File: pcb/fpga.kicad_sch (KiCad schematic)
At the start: 0 parts

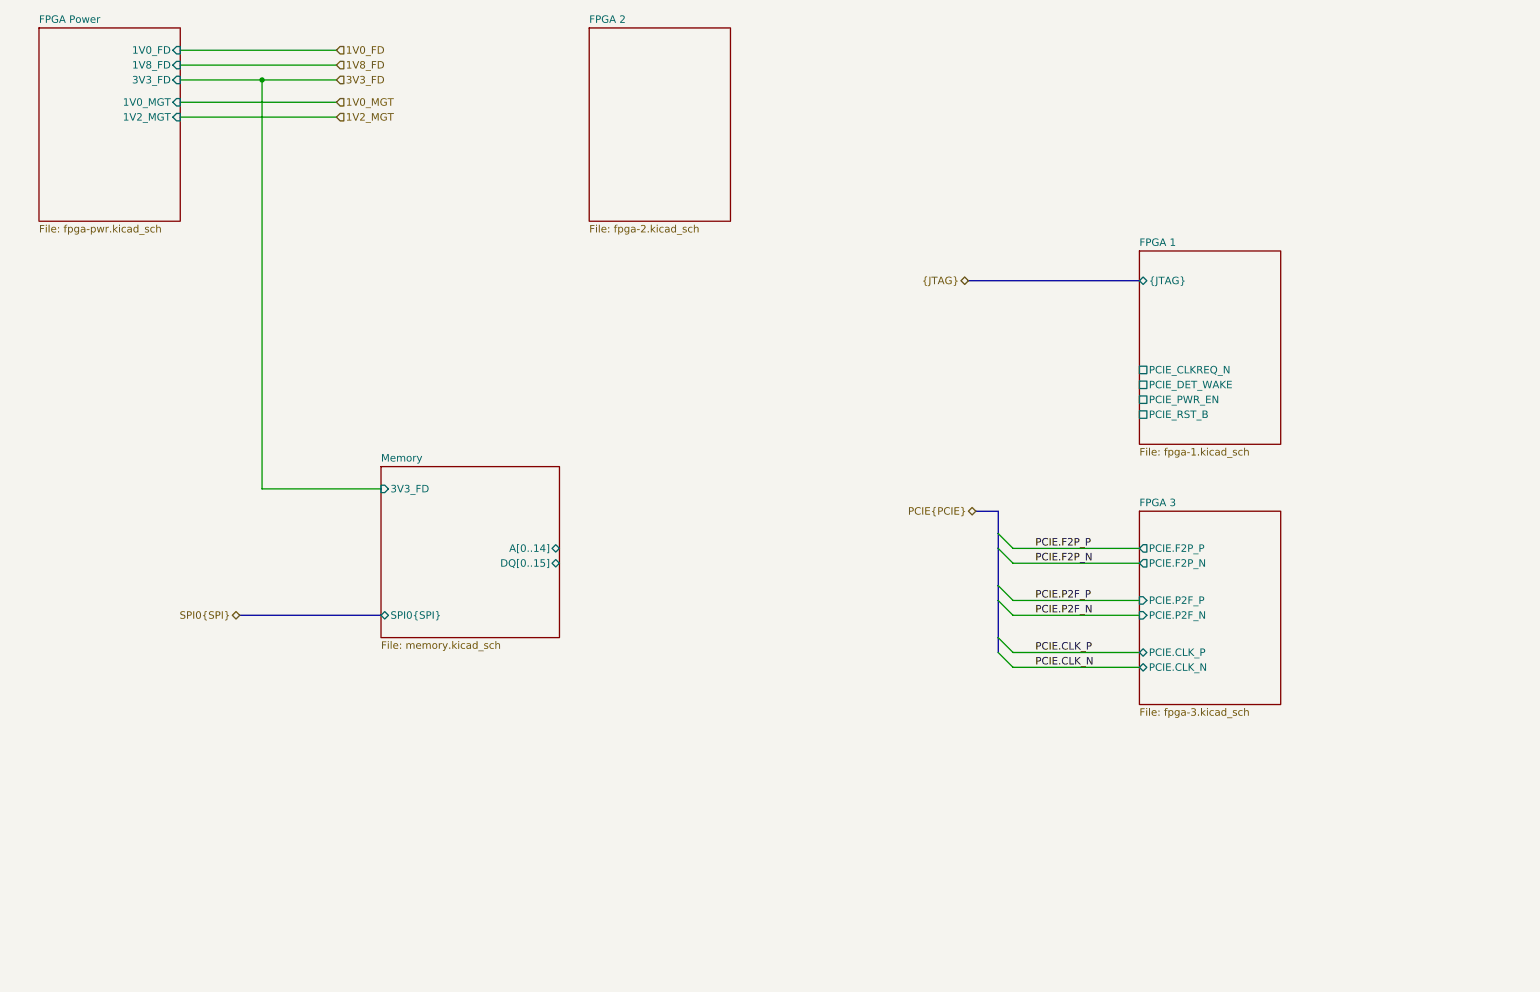
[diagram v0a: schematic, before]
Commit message: hierarchy and power sequencing, level shift
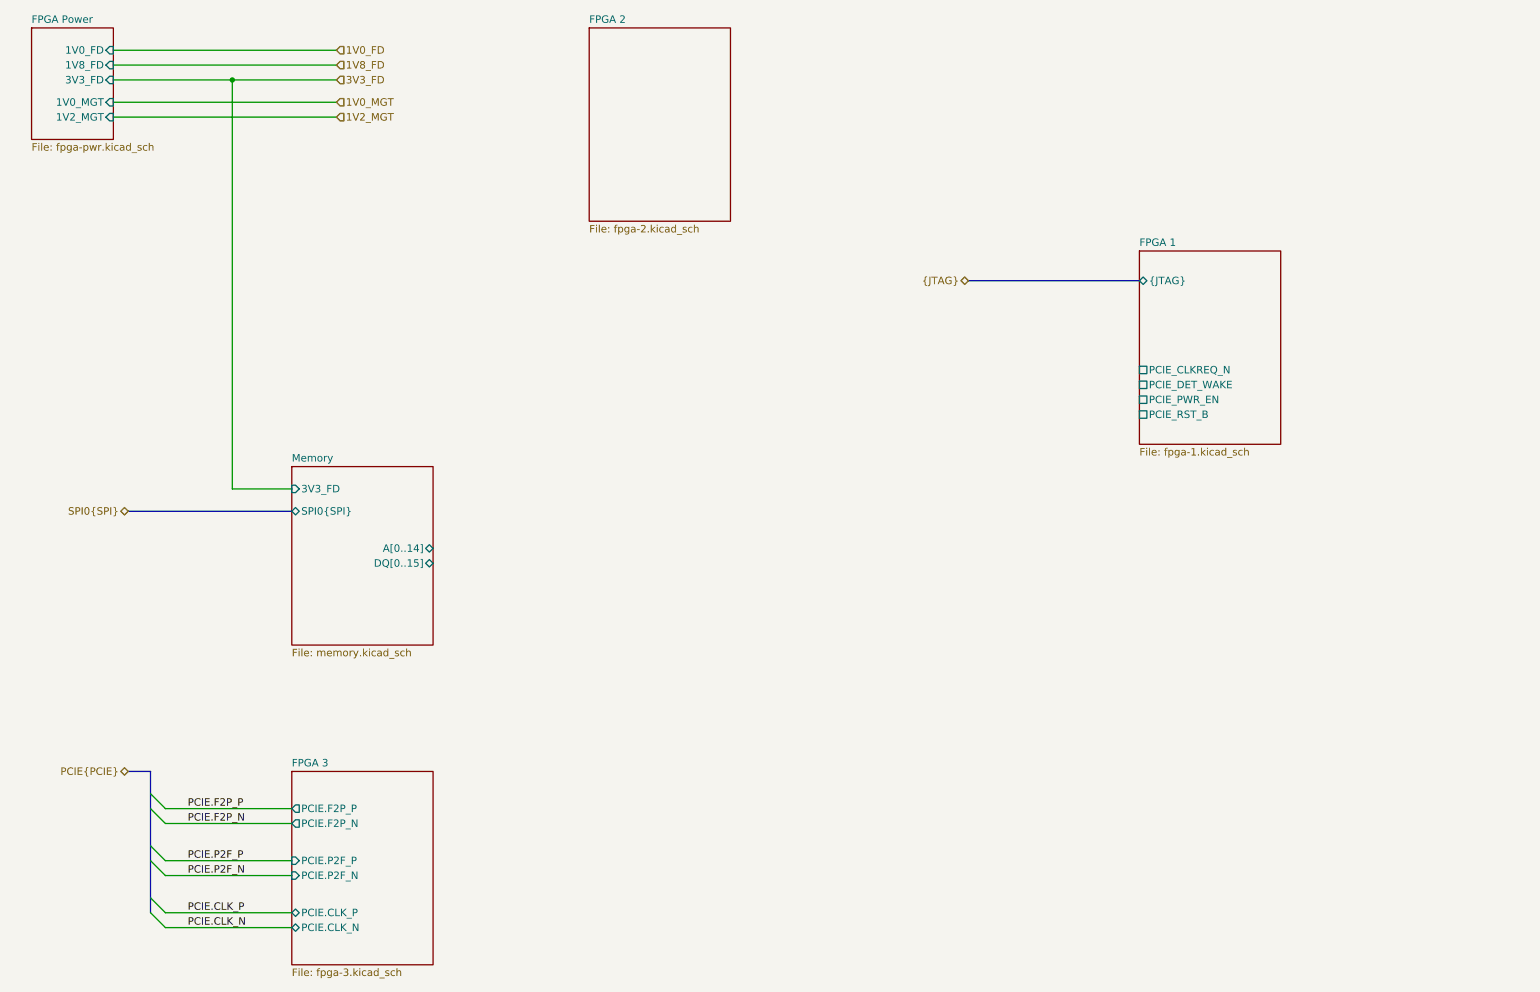
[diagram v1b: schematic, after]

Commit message: added hierarchical sheet, pwr seq
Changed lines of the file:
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@@
 	(bus
 		(pts
-			(xy 38.1 146.05) (xy 38.1 149.86)
+			(xy 38.1 132.08) (xy 38.1 149.86)
 		)
 		(stroke
@@
 	(bus
 		(pts
-			(xy 34.29 146.05) (xy 38.1 146.05)
+			(xy 34.29 132.08) (xy 38.1 132.08)
 		)
 		(stroke
@@
 		)
 	)
+	(hierarchical_label "PCIE.RST_B"
+		(shape input)
+		(at 34.29 134.62 180)
+		(effects
+			(font
+				(size 1.27 1.27)
+			)
+			(justify right)
+		)
+	)
 	(hierarchical_label "1V2_MGT"
 		(shape input)
@@
 	(hierarchical_label "PCIE{PCIE}"
 		(shape bidirectional)
-		(at 34.29 146.05 180)
+		(at 34.29 132.08 180)
 		(effects
 			(font

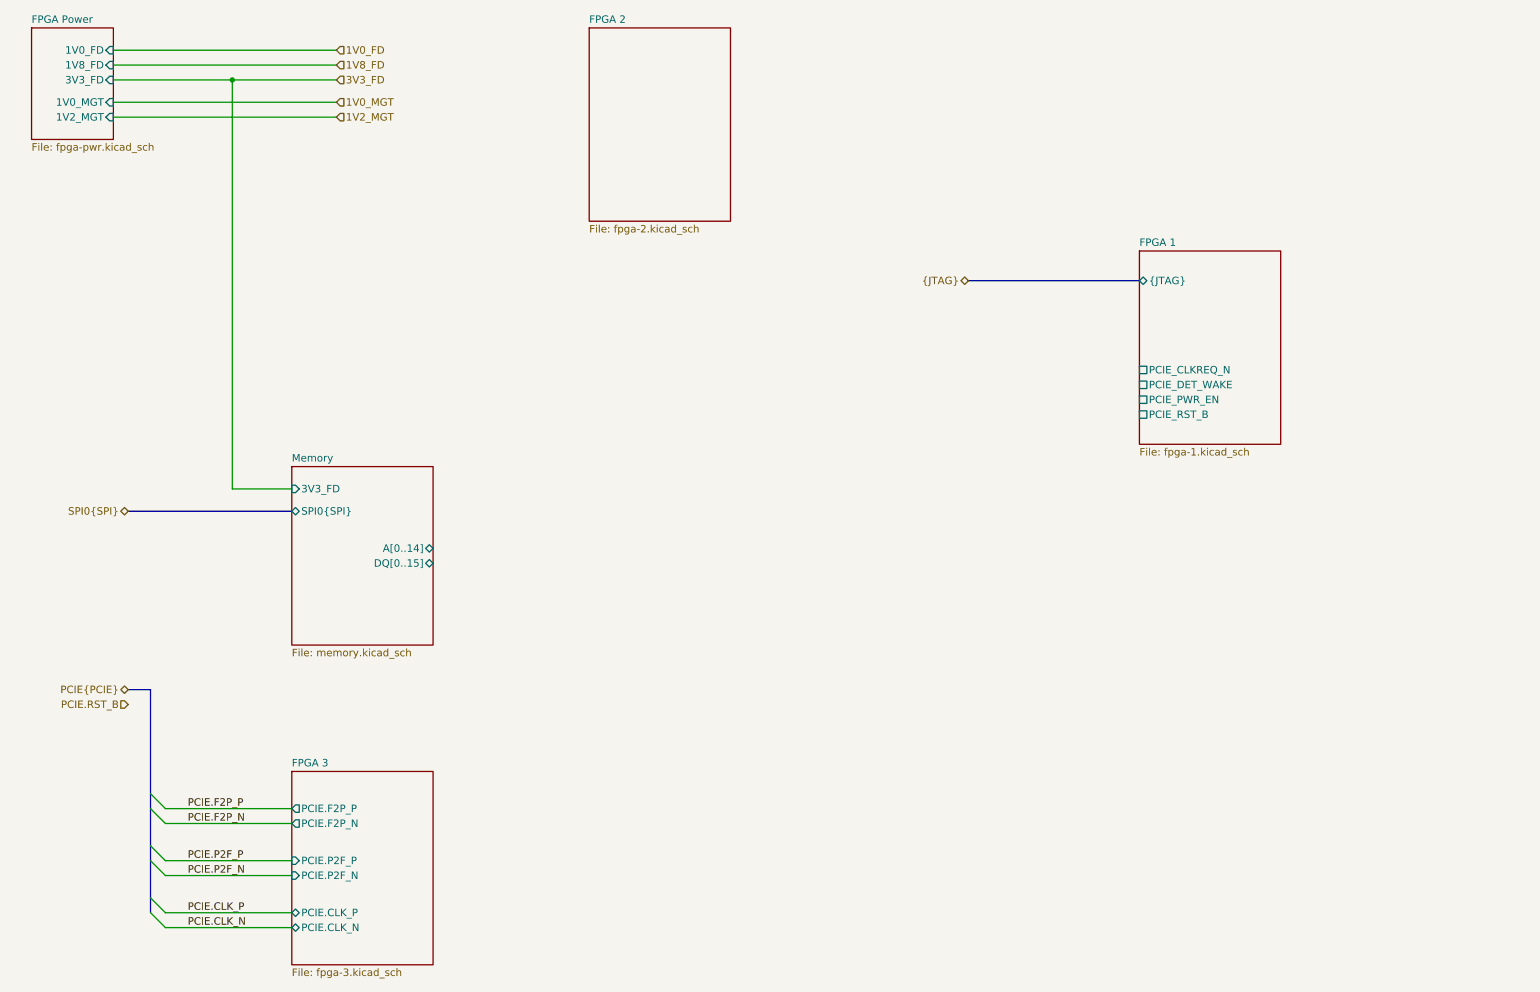
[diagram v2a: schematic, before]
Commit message: defined memory pinouts
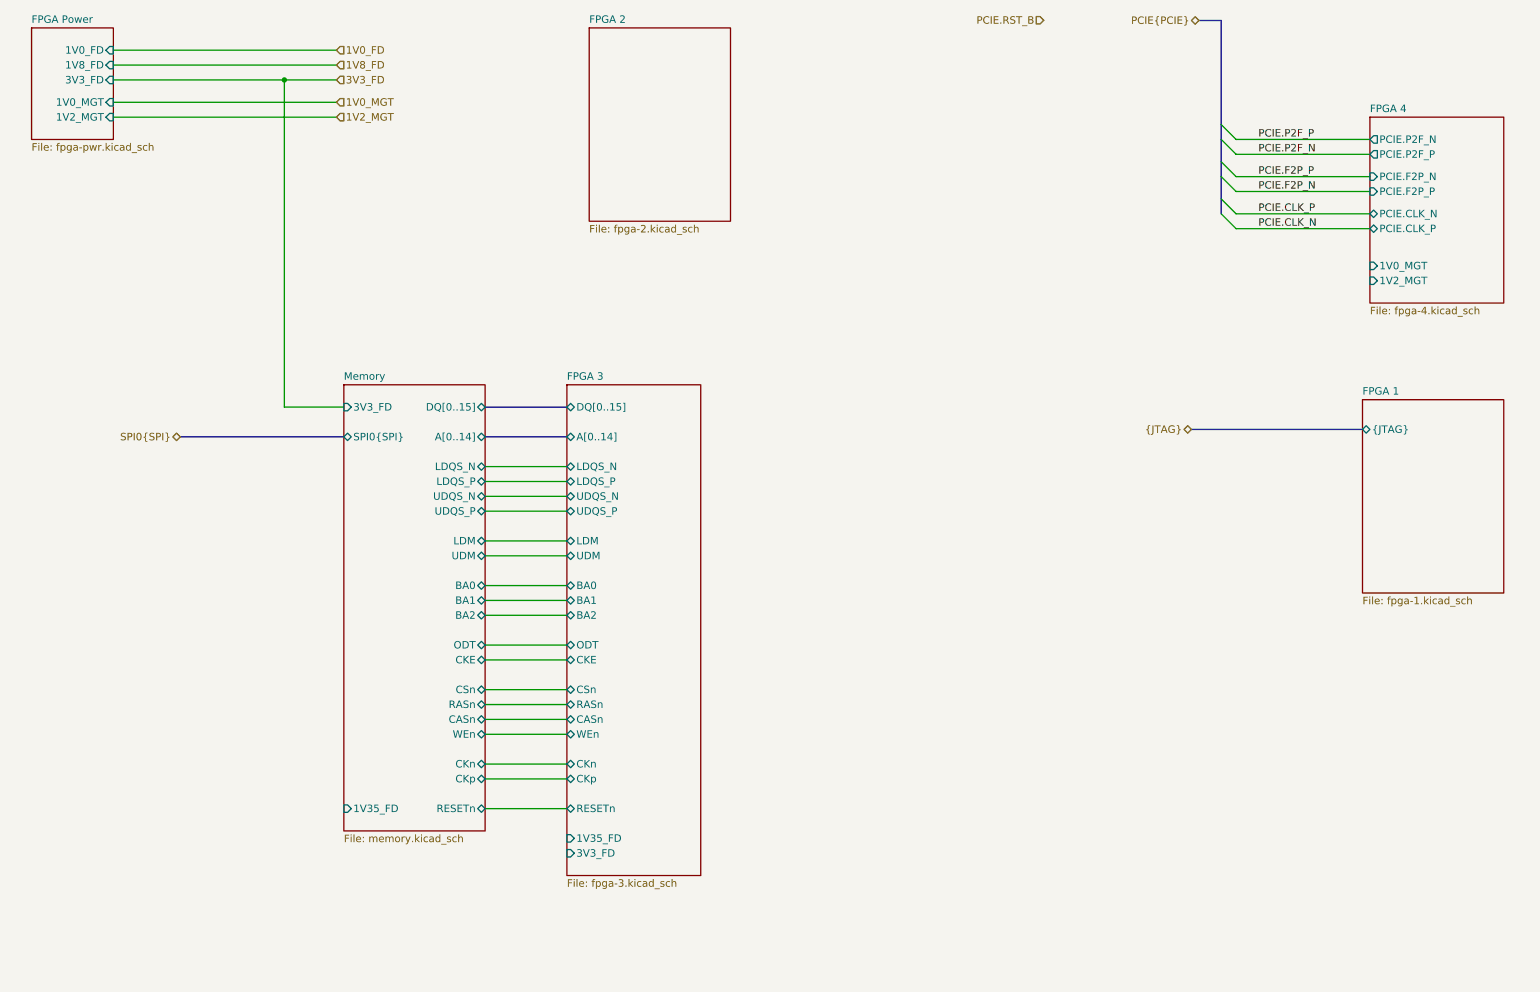
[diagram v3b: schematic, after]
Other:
- added sheet FPGA 4 (fpga-4.kicad_sch)
- sheet FPGA 1 ports: added none; removed PCIE_CLKREQ_N, PCIE_DET_WAKE, PCIE_PWR_EN, PCIE_RST_B
- sheet FPGA 3 ports: added 1V35_FD, 3V3_FD, A[0..14], BA0, BA1, BA2, CASn, CKE, CKn, CKp, CSn, DQ[0..15], LDM, LDQS_N, LDQS_P, ODT, RASn, RESETn, UDM, UDQS_N, UDQS_P, WEn; removed PCIE.CLK_N, PCIE.CLK_P, PCIE.F2P_N, PCIE.F2P_P, PCIE.P2F_N, PCIE.P2F_P
- sheet Memory ports: added 1V35_FD, BA0, BA1, BA2, CASn, CKE, CKn, CKp, CSn, LDM, LDQS_N, LDQS_P, ODT, RASn, RESETn, UDM, UDQS_N, UDQS_P, WEn; removed none
